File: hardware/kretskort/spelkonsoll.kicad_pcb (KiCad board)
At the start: 2 copper layers, 176.6 x 56.6 mm, 29 parts, among them SW1 B3F-1052, SW1 SW_Push, SW2 B3F-1052, SW2 SW_Push, SW3 B3F-1052, SW3 SW_Push, SW4 B3F-1052, SW4 SW_Push, SW5 B3F-1052, SW5 SW_Push, SW6 B3F-1052, SW6 SW_Push, SW7 B3F-1052, SW7 SW_Push, SW8 B3F-1052, SW8 SW_Push, U1 ESP32-DEVKITC-32D, U2 ILI9488, U3 1043

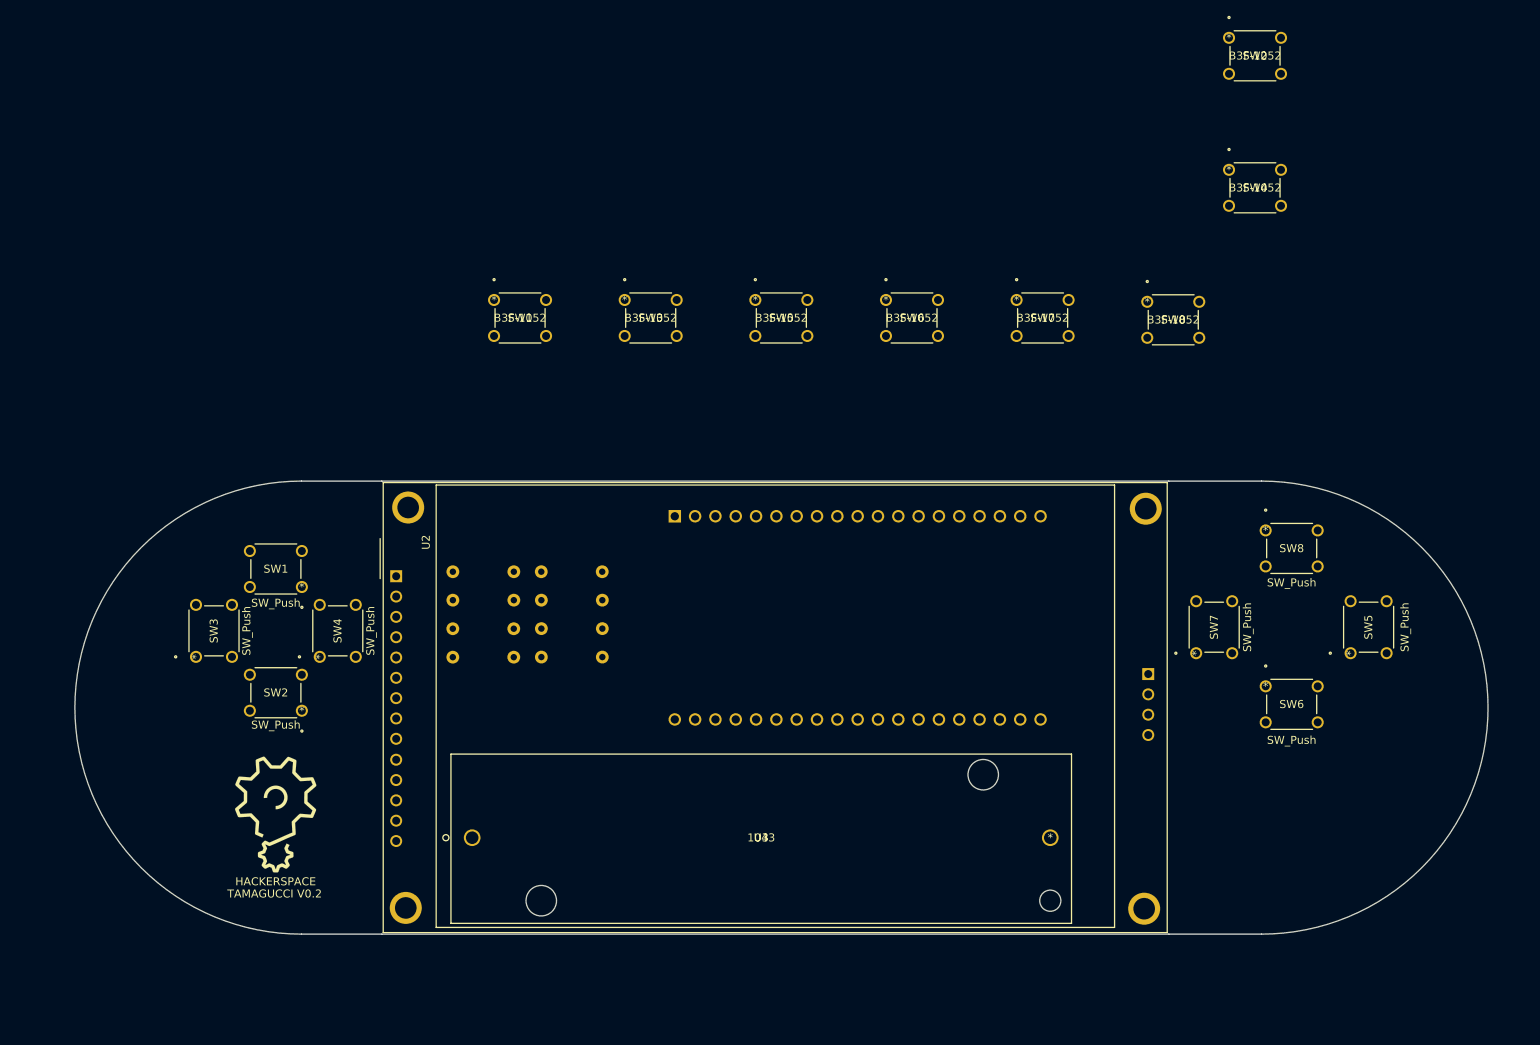
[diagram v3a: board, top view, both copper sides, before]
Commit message: update schematic and footprints
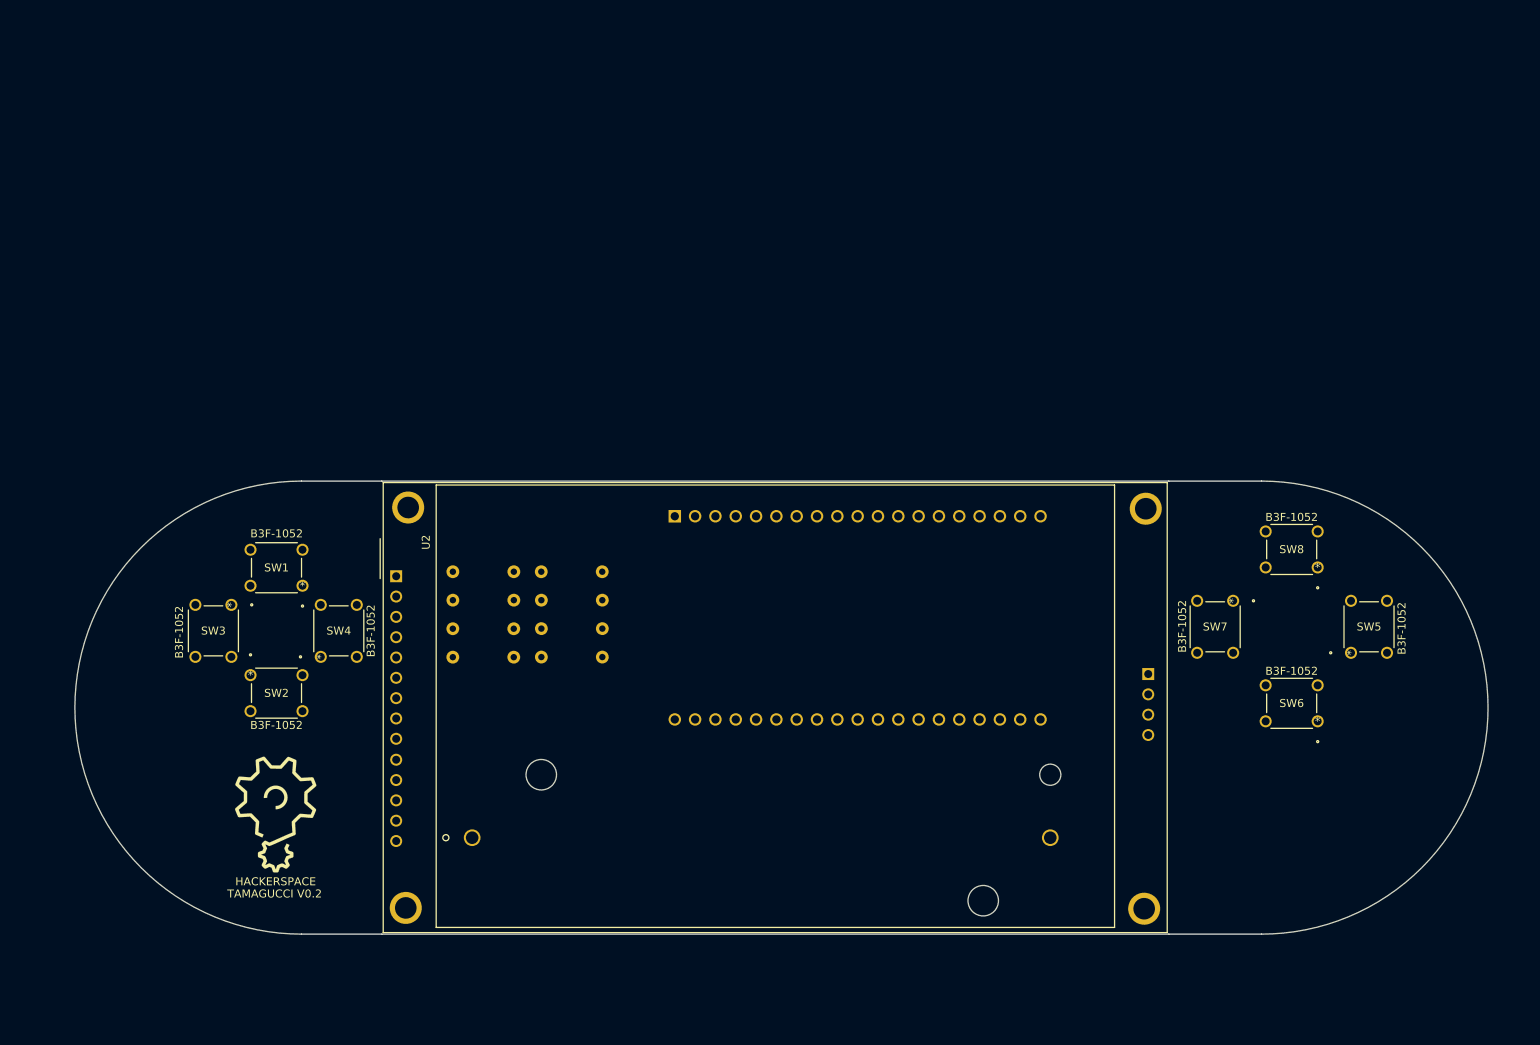
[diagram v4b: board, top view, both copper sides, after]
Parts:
- removed the SW1 at (86.3, 82.5)
- removed the SW1 at (110.3, 46.6)
- removed the SW2 at (86.3, 97.9)
- removed the SW3 at (73.0, 91.2)
- removed the SW3 at (126.6, 46.6)
- removed the SW4 at (88.5, 91.2)
- removed the SW4 at (202.2, 30.3)
- removed the SW5 at (217.4, 90.7)
- removed the SW6 at (206.8, 94.9)
- removed the SW7 at (198.1, 90.7)
- removed the SW8 at (206.8, 75.4)
- removed the SW8 at (192.0, 46.8)
- added SW1: B3F-1052, footprints:Button, F.Cu at (86.4, 82.3)
- added SW3: B3F-1052, footprints:Button, F.Cu at (77.5, 84.7)
- added SW4: B3F-1052, footprints:Button, F.Cu at (88.6, 91.2)
- added SW8: B3F-1052, footprints:Button, F.Cu at (213.3, 80.0)
- U3: moved to B.Cu
- moved SW2 146.0 mm to (79.9, 93.5)
- moved SW5 86.5 mm to (217.4, 90.7), turned to 90 degrees
- moved SW6 75.4 mm to (213.3, 99.2), turned to 180 degrees
- moved SW7 46.3 mm to (202.7, 84.2), turned to 270 degrees
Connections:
- R1 pad 1: +5V -> BTN_DP_UP
- SW2 pad 1: BTN_DP_DOWN -> +5V
- SW2 pad 3: +5V -> BTN_DP_DOWN
- SW5 pad 1: BTN_A -> +5V
- SW5 pad 3: +5V -> BTN_A
- SW6 pad 1: BTN_B -> +5V
- SW6 pad 3: +5V -> BTN_B
- SW7 pad 1: BTN_X -> +5V
- SW7 pad 3: +5V -> BTN_X
- U3 pad 1: +5V -> GND
- U3 pad 2: GND -> +5V

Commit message: added power switch
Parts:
- added SW9: SW_DPDT_x2, footprints:PowerButton, B.Cu at (112.8, 71.9)
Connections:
- U3 pad 2: +5V -> Net-(SW9-Pad2)
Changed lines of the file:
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@@
     (tracks 5)
     (zones 0)
-    (modules 21)
-    (nets 62)
+    (modules 22)
+    (nets 64)
   )
   (page A4)
@@
   (net 60 "Net-(SW8-Pad2)")
   (net 61 "Net-(SW8-Pad4)")
+  (net 62 "Net-(SW9-Pad2)")
+  (net 63 "Net-(SW9-Pad3)")
   (net_class Default "This is the default net class."
     (clearance 0.2)
@@
     (add_net "Net-(SW8-Pad2)")
     (add_net "Net-(SW8-Pad4)")
+    (add_net "Net-(SW9-Pad2)")
+    (add_net "Net-(SW9-Pad3)")
     (add_net "Net-(U1-Pad1)")
     (add_net "Net-(U1-Pad13)")
@@
     (pad 3 np_thru_hole circle (at -8.382 7.874) (size 3.81 3.81) (drill 3.81) (layers *.Cu *.Mask))
     (pad 2 thru_hole circle (at 0 0) (size 2.0828 2.0828) (drill 1.5748) (layers *.Cu *.Mask)
-      (net 1 +5V))
+      (net 62 "Net-(SW9-Pad2)"))
     (pad 1 thru_hole circle (at -72.263 0) (size 2.0828 2.0828) (drill 1.5748) (layers *.Cu *.Mask)
       (net 2 GND))
@@
       (at (xyz 0 0 0))
       (scale (xyz 1 1 1))
+      (rotate (xyz 0 0 0))
+    )
+  )
+  (module footprints:PowerButton (layer B.Cu)
+    (at 112.776 71.882)
+    (descr "CuK miniature slide switch, OS series, SPDT, right angle, http://www.ckswitches.com/media/1428/os.pdf")
+    (tags "switch SPDT")
+    (fp_text reference SW9 (at 1.4 3.6) (layer B.SilkS)
+      (effects (font (size 1 1) (thickness 0.15)) (justify mirror))
+    )
+    (fp_text value SW_DPDT_x2 (at 1.7 -7.7) (layer B.Fab)
+      (effects (font (size 1 1) (thickness 0.15)) (justify mirror))
+    )
+    (fp_line (start -3.7 2.7) (end 7.7 2.7) (layer B.CrtYd) (width 0.05))
+    (fp_line (start -3.7 -6.7) (end -3.7 2.7) (layer B.CrtYd) (width 0.05))
+    (fp_line (start 7.7 -6.7) (end -3.7 -6.7) (layer B.CrtYd) (width 0.05))
+    (fp_line (start 7.7 2.7) (end 7.7 -6.7) (layer B.CrtYd) (width 0.05))
+    (fp_line (start 4 -2.3) (end 6.3 -2.3) (layer B.SilkS) (width 0.15))
+    (fp_line (start -2.3 -2.3) (end -0.1 -2.3) (layer B.SilkS) (width 0.15))
+    (fp_line (start -2.3 2.3) (end 6.3 2.3) (layer B.SilkS) (width 0.15))
+    (fp_line (start 0 -6.2) (end 0 -2.2) (layer B.Fab) (width 0.1))
+    (fp_line (start 2 -6.2) (end 0 -6.2) (layer B.Fab) (width 0.1))
+    (fp_line (start 2 -2.2) (end 2 -6.2) (layer B.Fab) (width 0.1))
+    (fp_line (start 6.3 -2.2) (end 6.3 2.2) (layer B.Fab) (width 0.1))
+    (fp_line (start -2.3 -2.2) (end 6.3 -2.2) (layer B.Fab) (width 0.1))
+    (fp_line (start -2.3 2.2) (end -2.3 -2.2) (layer B.Fab) (width 0.1))
+    (fp_line (start -2.3 2.2) (end 6.3 2.2) (layer B.Fab) (width 0.1))
+    (fp_text user %R (at 2.3 -1.7) (layer B.Fab)
+      (effects (font (size 0.5 0.5) (thickness 0.1)) (justify mirror))
+    )
+    (pad 1 thru_hole rect (at 0 0) (size 1.5 2.5) (drill 0.9) (layers *.Cu *.Mask)
+      (net 1 +5V))
+    (pad 2 thru_hole oval (at 2 0) (size 1.5 2.5) (drill 0.9) (layers *.Cu *.Mask)
+      (net 62 "Net-(SW9-Pad2)"))
+    (pad 3 thru_hole oval (at 4 0) (size 1.5 2.5) (drill 0.9) (layers *.Cu *.Mask)
+      (net 63 "Net-(SW9-Pad3)"))
+    (pad "" thru_hole oval (at -2.1 0) (size 2.2 3.5) (drill 1.5) (layers *.Cu *.Mask))
+    (pad "" thru_hole oval (at 6.1 0) (size 2.2 3.5) (drill 1.5) (layers *.Cu *.Mask))
+    (model ${KISYS3DMOD}/Button_Switch_THT.3dshapes/SW_CuK_OS102011MA1QN1_SPDT_Angled.wrl
+      (at (xyz 0 0 0))
+      (scale (xyz 1 1 1))

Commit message: glemte å lagre :(
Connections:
- SW9 pad 1: +5V -> Net-(SW9-Pad1)
- SW9 pad 3: Net-(SW9-Pad3) -> +5V

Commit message: må slutte å glemme å lagre :(
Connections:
- U1 pad 1: Net-(U1-Pad1) -> +5V
- U1 pad 19: +5V -> Net-(U1-Pad19)
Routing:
- net +5V: track 0.02 -> 247.4 mm
- net Net-(SW9-Pad2): track 0.00 -> 198.0 mm
- net GND: track 0.13 -> 154.6 mm, vias 0 -> 3
- net BTN_DP_LEFT: track 0.00 -> 109.0 mm
- net BTN_DP_UP: track 0.00 -> 105.3 mm
- net BTN_DP_RIGHT: track 0.00 -> 95.1 mm, vias 0 -> 2
- net BTN_DP_DOWN: track 0.00 -> 88.5 mm
- net BTN_A: track 0.00 -> 83.5 mm
- net RESET: track 0.00 -> 75.9 mm
- net BTN_B: track 0.00 -> 74.8 mm
- net CS: track 0.00 -> 68.1 mm
- net BTN_Y: track 0.00 -> 63.6 mm
- net DC\RS: track 0.00 -> 63.4 mm
- net SCK: track 0.00 -> 57.6 mm, vias 0 -> 2
- net MISO: track 0.00 -> 53.6 mm
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- added copper zone on B.Cu, net GND
- added copper zone on F.Cu, net GND
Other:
- rule pad_to_mask_clearance: 0.051 -> 0
